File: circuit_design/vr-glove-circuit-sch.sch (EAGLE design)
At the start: 34 parts, among them T1 N-CHANNEL-MOSFET-BSS138, T2 N-CHANNEL-MOSFET-BSS138, T3 N-CHANNEL-MOSFET-BSS138, T4 N-CHANNEL-MOSFET-BSS138, T5 N-CHANNEL-MOSFET-BSS138, T6 N-CHANNEL-MOSFET-BSS138, U1 ARDUINO_SHIELDNO_SILK

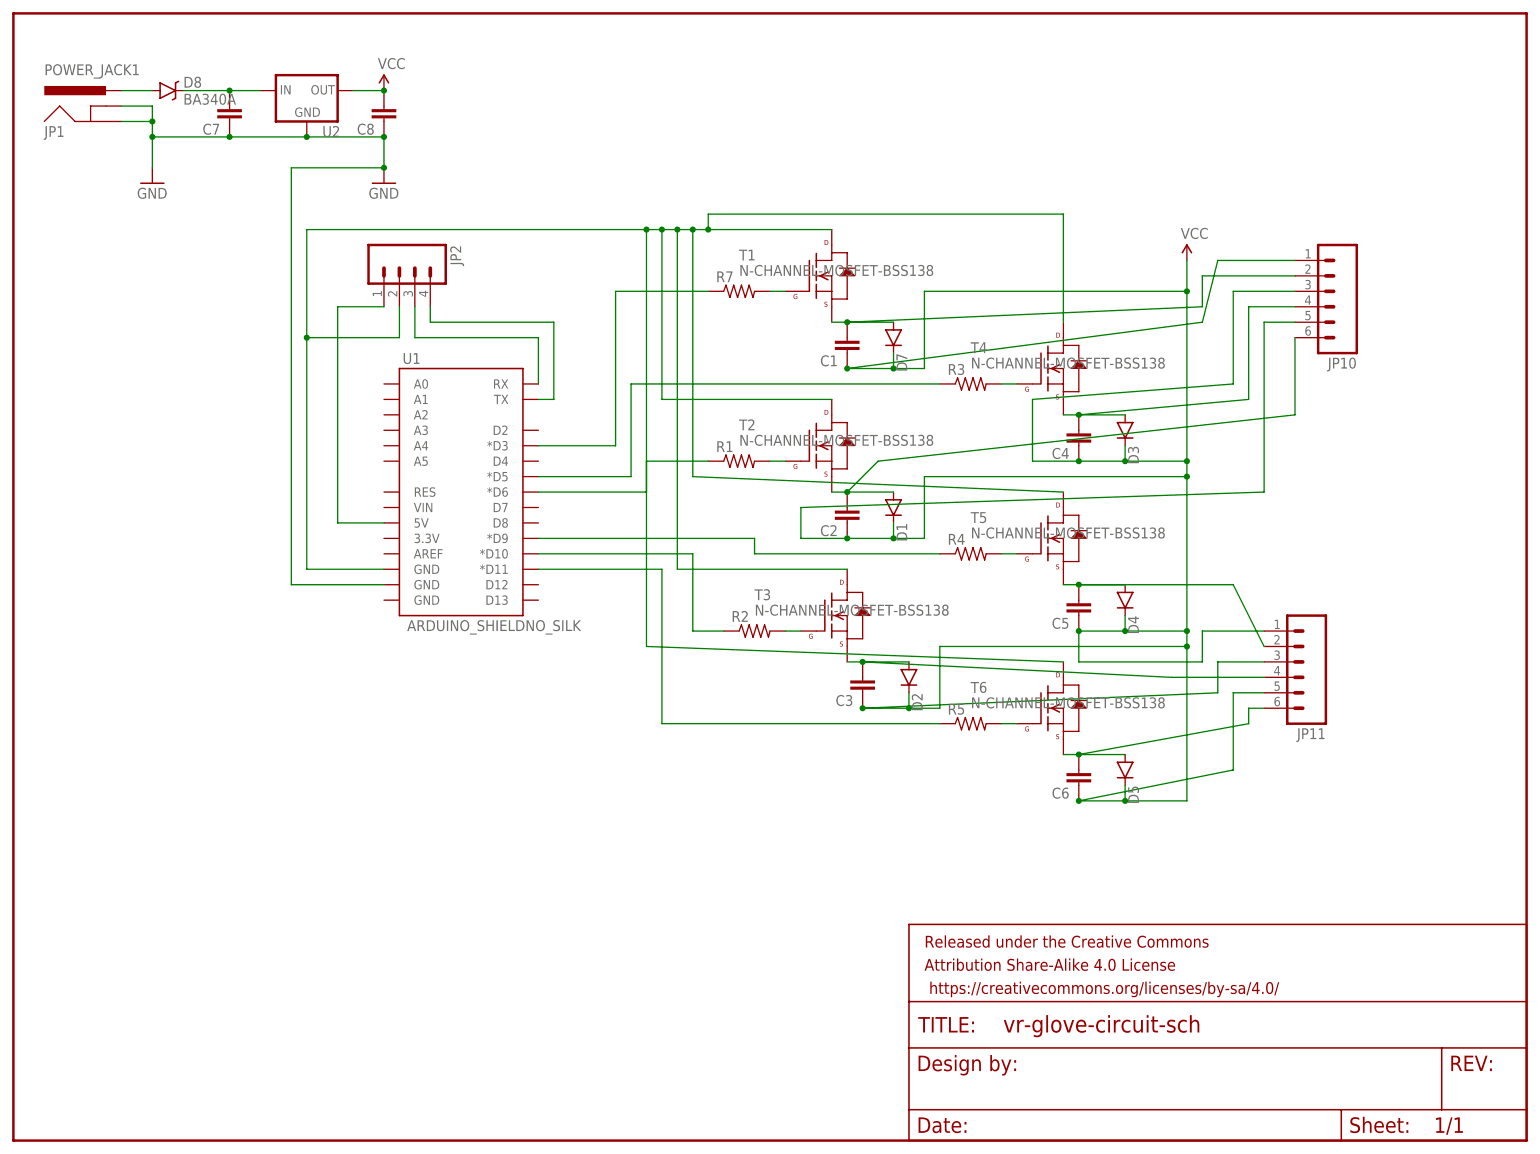
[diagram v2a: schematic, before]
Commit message: working wireless communication
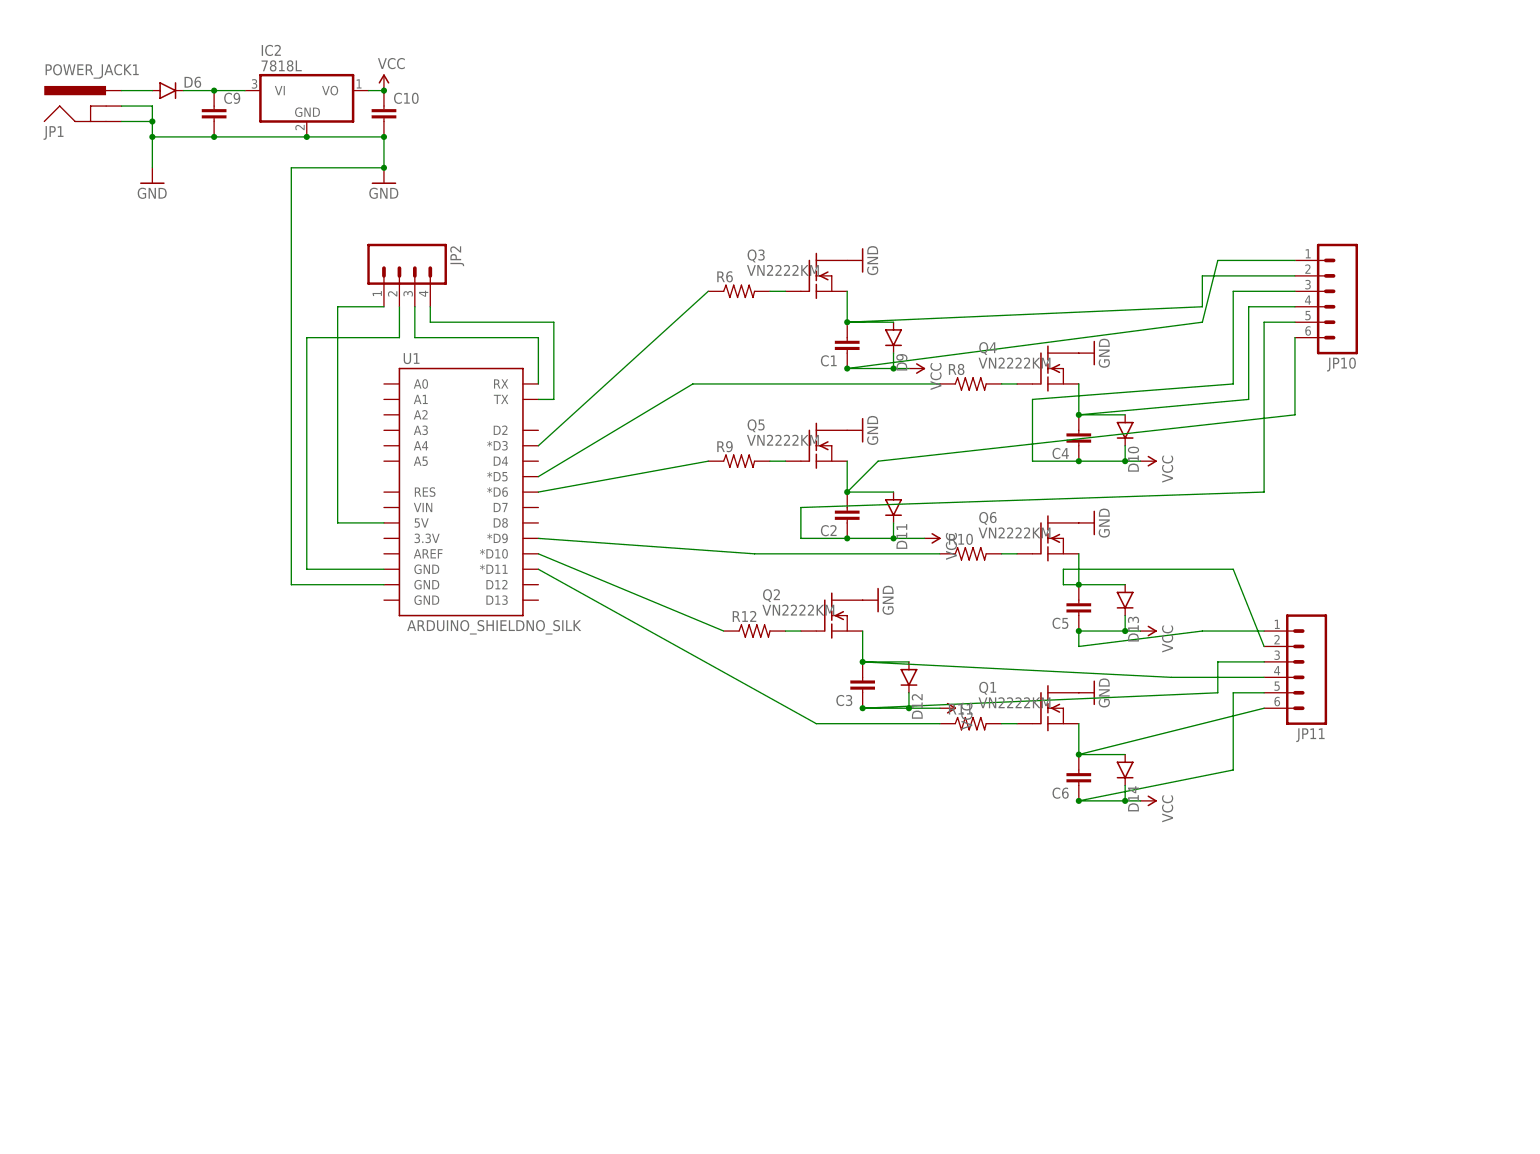
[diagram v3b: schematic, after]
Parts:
- removed C7, C8: (no value), SparkFun-Capacitors:CAP0402-CAP
- removed D1, D2, D3, D4, D5, D7: (no value), SparkFun-DiscreteSemi:DIODESMA
- removed D8: BA340A, SparkFun-DiscreteSemi:B340A
- removed FRAME1: (no value), SparkFun-Aesthetics:FRAME-LETTER
- removed R1, R2, R3, R4, R5, R7: (no value), SparkFun-Resistors:RESISTORPTH-1/2W
- removed T1, T2, T3, T4, T5, T6: N-CHANNEL-MOSFET-BSS138, GeekAmmo:N-CHANNEL-MOSFET-BSS138
- removed U2: (no value), SparkFun-PowerIC:V_REG_78XXSIDE
- added C10, C9: (no value), SparkFun-Passives:CAPPTH
- added D10, D11, D12, D13, D14, D6, D9: (no value), SparkFun-DiscreteSemi:DIODE1N4148
- added IC2: 7818L, linear:7818L
- added Q1, Q2, Q3, Q4, Q5, Q6: VN2222KM, transistor-fet:VN2222KM
- added R10, R11, R12, R6, R8, R9: (no value), SparkFun-Resistors:RESISTORPTH-1/4W-VERT
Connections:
- removed net N$25: C7.2, D8.C, U2.IN
- new net N$18: C9.1, D6.C, IC2.VI
- net GND: now also C10.2, C9.2, IC2.GND, Q1.D, Q2.D, Q3.D, Q4.D, Q5.D, Q6.D; no longer C7.1, C8.1, U2.GND
- net N$1: now also Q3.G, R6.2; no longer R7.2, T1.G
- net N$10: now also Q4.G, R8.2; no longer R3.2, T4.G
- net N$11: now also D10.A, Q4.S; no longer D3.A, T4.S
- net N$13: now also Q6.G, R10.2; no longer R4.2, T5.G
- net N$14: now also D13.A, Q6.S; no longer D4.A, T5.S
- net N$16: now also Q1.G, R11.2; no longer R5.2, T6.G
- net N$17: now also D14.A, Q1.S; no longer D5.A, T6.S
- net N$19: now also R6.1; no longer R7.1
- net N$2: now also D9.A, Q3.S; no longer D7.A, T1.S
- net N$20: now also R8.1; no longer R3.1
- net N$21: now also R9.1; no longer R1.1
- net N$22: now also R10.1; no longer R4.1
- net N$23: now also R12.1; no longer R2.1
- net N$24: now also R11.1; no longer R5.1
- net N$3: no longer T1.D, T2.D, T3.D, T4.D, T5.D, T6.D
- net N$4: now also Q5.G, R9.2; no longer R1.2, T2.G
- net N$5: now also D11.A, Q5.S; no longer D1.A, T2.S
- net N$7: now also Q2.G, R12.2; no longer R2.2, T3.G
- net N$8: now also D12.A, Q2.S; no longer D2.A, T3.S
- net N$9: now also D6.A; no longer D8.A
- net VCC: now also C10.1, D10.C, D11.C, D12.C, D13.C, D14.C, D9.C, IC2.VO; no longer C8.2, D1.C, D2.C, D3.C, D4.C, D5.C, D7.C, U2.OUT
